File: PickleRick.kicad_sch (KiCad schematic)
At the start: 56 parts, among them J1 RBUS, J12 Conn_01x03_Male, J2 Conn_01x02_Male, J3 292227-7, J4 Micro_SD_Card_Det, Q1 PMV20ENR, U1 ESP32-S3, U2 DPS310, Y1 40MHz±10ppm

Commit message: all components basically routed and fitted onto pickle v2
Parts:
- R34, R35: footprint (none) -> Resistor_SMD:R_0402_1005Metric
- U2: footprint XDCR_DPS310 -> iclr:XDCR_DPS310
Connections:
- net BARO_CS: now also U1.19 (GPIO14/ADC2_CH3); no longer U1.12 (GPIO7/ADC1_CH6)
- net HSPI_MISO: now also U1.39 (GPIO34); no longer U1.40 (GPIO35)
- net HSPI_MOSI: now also U1.38 (GPIO33); no longer U1.39 (GPIO34)
- net HSPI_SCLK: now also U1.40 (GPIO35); no longer U1.38 (GPIO33)
- net IMU1_CS: now also U1.17 (GPIO12/ADC2_CH1); no longer U1.11 (GPIO6/ADC1_CH5)
- net IMU2_CS: now also U1.16 (GPIO11/ADC2_CH0); no longer U1.10 (GPIO5/ADC1_CH4)
- net LORA_CS: now also U1.15 (GPIO10/ADC1_CH9); no longer U1.13 (GPIO8/ADC1_CH7)
- net LORA_INT: now also U1.10 (GPIO5/ADC1_CH4); no longer U1.15 (GPIO10/ADC1_CH9)
- net MAG_CS: now also U1.18 (GPIO13/ADC2_CH2); no longer U1.9 (GPIO4/ADC1_CH3)
- net SD1_CS: now also U1.9 (GPIO4/ADC1_CH3); no longer U1.19 (GPIO14/ADC2_CH3)
- net SD1_DET: now also U1.11 (GPIO6/ADC1_CH5); no longer U1.18 (GPIO13/ADC2_CH2)
- net SD2_CS: now also U1.13 (GPIO8/ADC1_CH7); no longer U1.17 (GPIO12/ADC2_CH1)
- net SD2_DET: now also U1.12 (GPIO7/ADC1_CH6); no longer U1.16 (GPIO11/ADC2_CH0)
- net VSPI_MISO: now also J3.6, U1.43 (GPIO38); no longer J3.3, U1.41 (GPIO36)
- net VSPI_MOSI: now also J3.3, U1.41 (GPIO36); no longer J3.6, U1.43 (GPIO38)
- net power/RBUS_3.3_IN renamed power/RBUS_3.3V_IN
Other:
- sheet power ports: added RBUS_3.3V_IN; removed RBUS_3.3_IN
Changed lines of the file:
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@@
     (effects (font (size 1.27 1.27)) (justify left bottom))
   )
-  (label "IMU1_CS" (at 60.96 85.09 180)
+  (label "SD1_DET" (at 60.96 85.09 180)
     (effects (font (size 1.27 1.27)) (justify right bottom))
   )
@@
     (effects (font (size 1.27 1.27)) (justify left bottom))
   )
-  (label "VSPI_MISO" (at 243.84 30.48 0)
-    (effects (font (size 1.27 1.27)) (justify left bottom))
-  )
-  (label "SD2_CS" (at 60.96 100.33 180)
-    (effects (font (size 1.27 1.27)) (justify right bottom))
-  )
-  (label "LORA_INT" (at 60.96 95.25 180)
+  (label "VSPI_MOSI" (at 243.84 30.48 0)
+    (effects (font (size 1.27 1.27)) (justify left bottom))
+  )
+  (label "IMU1_CS" (at 60.96 100.33 180)
+    (effects (font (size 1.27 1.27)) (justify right bottom))
+  )
+  (label "LORA_CS" (at 60.96 95.25 180)
     (effects (font (size 1.27 1.27)) (justify right bottom))
   )
@@
     (effects (font (size 1.27 1.27)) (justify left bottom))
   )
-  (label "VSPI_MISO" (at 143.51 102.87 0)
+  (label "VSPI_MOSI" (at 143.51 102.87 0)
     (effects (font (size 1.27 1.27)) (justify left bottom))
   )
@@
     (effects (font (size 1.27 1.27)) (justify left bottom))
   )
-  (label "MAG_CS" (at 60.96 80.01 180)
+  (label "SD1_CS" (at 60.96 80.01 180)
     (effects (font (size 1.27 1.27)) (justify right bottom))
   )
@@
     (effects (font (size 1.27 1.27)) (justify left bottom))
   )
-  (label "VSPI_MOSI" (at 143.51 107.95 0)
+  (label "VSPI_MISO" (at 143.51 107.95 0)
     (effects (font (size 1.27 1.27)) (justify left bottom))
   )
@@
     (effects (font (size 1.27 1.27)) (justify left bottom))
   )
-  (label "HSPI_SCLK" (at 143.51 95.25 0)
-    (effects (font (size 1.27 1.27)) (justify left bottom))
-  )
-  (label "LORA_CS" (at 60.96 90.17 180)
+  (label "HSPI_MOSI" (at 143.51 95.25 0)
+    (effects (font (size 1.27 1.27)) (justify left bottom))
+  )
+  (label "SD2_CS" (at 60.96 90.17 180)
     (effects (font (size 1.27 1.27)) (justify right bottom))
   )
@@
     (effects (font (size 1.27 1.27)) (justify left bottom))
   )
-  (label "HSPI_MISO" (at 143.51 100.33 0)
+  (label "HSPI_SCLK" (at 143.51 100.33 0)
     (effects (font (size 1.27 1.27)) (justify left bottom))
   )
@@
     (effects (font (size 1.27 1.27)) (justify left bottom))
   )
-  (label "IMU2_CS" (at 60.96 82.55 180)
-    (effects (font (size 1.27 1.27)) (justify right bottom))
-  )
-  (label "HSPI_MOSI" (at 143.51 97.79 0)
-    (effects (font (size 1.27 1.27)) (justify left bottom))
-  )
-  (label "BARO_CS" (at 60.96 87.63 180)
+  (label "LORA_INT" (at 60.96 82.55 180)
+    (effects (font (size 1.27 1.27)) (justify right bottom))
+  )
+  (label "HSPI_MISO" (at 143.51 97.79 0)
+    (effects (font (size 1.27 1.27)) (justify left bottom))
+  )
+  (label "SD2_DET" (at 60.96 87.63 180)
     (effects (font (size 1.27 1.27)) (justify right bottom))
   )
@@
     (effects (font (size 1.27 1.27)) (justify right bottom))
   )
-  (label "SD1_CS" (at 60.96 105.41 180)
-    (effects (font (size 1.27 1.27)) (justify right bottom))
-  )
-  (label "VSPI_MOSI" (at 243.84 38.1 0)
+  (label "BARO_CS" (at 60.96 105.41 180)
+    (effects (font (size 1.27 1.27)) (justify right bottom))
+  )
+  (label "VSPI_MISO" (at 243.84 38.1 0)
     (effects (font (size 1.27 1.27)) (justify left bottom))
   )
@@
     (effects (font (size 1.27 1.27)) (justify left bottom))
   )
-  (label "SD2_DET" (at 60.96 97.79 180)
+  (label "IMU2_CS" (at 60.96 97.79 180)
     (effects (font (size 1.27 1.27)) (justify right bottom))
   )
@@
     (effects (font (size 1.27 1.27)) (justify left bottom))
   )
-  (label "SD1_DET" (at 60.96 102.87 180)
+  (label "MAG_CS" (at 60.96 102.87 180)
     (effects (font (size 1.27 1.27)) (justify right bottom))
   )
@@
       (effects (font (size 1.27 1.27)) (justify right))
     )
-    (property "Footprint" "" (id 2) (at 255.27 143.51 0)
+    (property "Footprint" "Resistor_SMD:R_0402_1005Metric" (id 2) (at 255.27 143.51 0)
       (effects (font (size 1.27 1.27)) hide)
     )
@@
       (effects (font (size 1.27 1.27)) (justify right))
     )
-    (property "Footprint" "" (id 2) (at 260.35 143.51 0)
+    (property "Footprint" "Resistor_SMD:R_0402_1005Metric" (id 2) (at 260.35 143.51 0)
       (effects (font (size 1.27 1.27)) hide)
     )
@@
     (property "Reference" "U2" (id 0) (at 250.19 102.87 0))
     (property "Value" "DPS310" (id 1) (at 250.19 105.41 0))
-    (property "Footprint" "XDCR_DPS310" (id 2) (at 250.19 120.65 0)
+    (property "Footprint" "iclr:XDCR_DPS310" (id 2) (at 250.19 120.65 0)
       (effects (font (size 1.27 1.27)) (justify bottom) hide)
     )
@@
       (effects (font (size 1.27 1.27)) (justify left))
     )
-    (pin "RBUS_3.3_IN" input (at 119.38 26.67 180)
+    (pin "RBUS_3.3V_IN" input (at 119.38 26.67 180)
       (effects (font (size 1.27 1.27)) (justify left))
     )
@@
     )
     (path "/ca0eab8e-e3fd-464d-bb03-d1603b8a651b/755f7a4b-a56d-4d46-9756-c8f6d0fad6ca"
-      (reference "R17") (unit 1) (value "500") (footprint "Resistor_SMD:R_0603_1608Metric")
+      (reference "R17") (unit 1) (value "500") (footprint "Resistor_SMD:R_0402_1005Metric")
     )
     (path "/ca0eab8e-e3fd-464d-bb03-d1603b8a651b/d2de353e-901e-432e-8627-a1b97e994765"
-      (reference "R18") (unit 1) (value "500") (footprint "Resistor_SMD:R_0603_1608Metric")
+      (reference "R18") (unit 1) (value "500") (footprint "Resistor_SMD:R_0402_1005Metric")
     )
     (path "/ca0eab8e-e3fd-464d-bb03-d1603b8a651b/09e6991d-9281-472b-b68c-4275861534b7"
@@
     )
     (path "/ca0eab8e-e3fd-464d-bb03-d1603b8a651b/c4d9bc73-27a3-45e8-9f5d-4537c1fd0ae5"
-      (reference "R21") (unit 1) (value "500") (footprint "Resistor_SMD:R_0603_1608Metric")
+      (reference "R21") (unit 1) (value "500") (footprint "Resistor_SMD:R_0402_1005Metric")
     )
     (path "/ca0eab8e-e3fd-464d-bb03-d1603b8a651b/24badbae-eef7-4d2c-a598-610e488ef81e"
-      (reference "R22") (unit 1) (value "500") (footprint "Resistor_SMD:R_0603_1608Metric")
+      (reference "R22") (unit 1) (value "500") (footprint "Resistor_SMD:R_0402_1005Metric")
     )
     (path "/ca0eab8e-e3fd-464d-bb03-d1603b8a651b/e4ae5c4e-e3f6-4ed9-b103-ab6e6ce37889"
@@
     )
     (path "/177d953f-3629-4fb8-8514-a9b0a91946a8"
-      (reference "R34") (unit 1) (value "4.7k") (footprint "")
+      (reference "R34") (unit 1) (value "4.7k") (footprint "Resistor_SMD:R_0402_1005Metric")
     )
     (path "/81f99459-3715-4203-a020-d8351a4eee55"
-      (reference "R35") (unit 1) (value "4.7k") (footprint "")
+      (reference "R35") (unit 1) (value "4.7k") (footprint "Resistor_SMD:R_0402_1005Metric")
     )
     (path "/c2e1c0d9-d402-4bd4-a6a0-62ddeebb3565"
@@
     )
     (path "/150d7a0e-7d8c-4788-bc30-4a3682bf4d09/268b5def-07ff-4842-bca3-d3886d833ee9"
-      (reference "TP10") (unit 1) (value "TestPoint") (footprint "TestPoint:TestPoint_Pad_D1.5mm")
+      (reference "TP10") (unit 1) (value "TestPoint") (footprint "TestPoint:TestPoint_Pad_D1.0mm")
     )
     (path "/150d7a0e-7d8c-4788-bc30-4a3682bf4d09/191a622e-bbb5-4124-b7c1-abd7ab78da85"
-      (reference "TP11") (unit 1) (value "TestPoint") (footprint "TestPoint:TestPoint_Pad_D1.5mm")
+      (reference "TP11") (unit 1) (value "TestPoint") (footprint "TestPoint:TestPoint_Pad_D1.0mm")
     )
     (path "/150d7a0e-7d8c-4788-bc30-4a3682bf4d09/6b63f8e0-062c-443a-b458-4bc92c46512c"
-      (reference "TP12") (unit 1) (value "TestPoint") (footprint "TestPoint:TestPoint_Pad_D1.5mm")
+      (reference "TP12") (unit 1) (value "TestPoint") (footprint "TestPoint:TestPoint_Pad_D1.0mm")
     )
     (path "/150d7a0e-7d8c-4788-bc30-4a3682bf4d09/0870865b-0b96-41ff-bd58-be45e025f47e"
-      (reference "TP13") (unit 1) (value "TestPoint") (footprint "TestPoint:TestPoint_Pad_D1.5mm")
+      (reference "TP13") (unit 1) (value "TestPoint") (footprint "TestPoint:TestPoint_Pad_D1.0mm")
     )
     (path "/150d7a0e-7d8c-4788-bc30-4a3682bf4d09/7ed4ea5d-2ecf-42be-88a1-8b4cc9b70ab6"
-      (reference "TP14") (unit 1) (value "TestPoint") (footprint "TestPoint:TestPoint_Pad_D1.5mm")
+      (reference "TP14") (unit 1) (value "TestPoint") (footprint "TestPoint:TestPoint_Pad_D1.0mm")
     )
     (path "/53a382a5-9123-45f3-a2e9-3b2de6ca541d/765637ac-b392-4de9-bfe2-ec35604f0b7c"
@@
     )
     (path "/a53547c8-4347-46fd-a668-dd224bf6ff89"
-      (reference "U2") (unit 1) (value "DPS310") (footprint "XDCR_DPS310")
+      (reference "U2") (unit 1) (value "DPS310") (footprint "iclr:XDCR_DPS310")
     )
     (path "/ca0eab8e-e3fd-464d-bb03-d1603b8a651b/c54e645d-6515-448d-a61f-0a3d4effdf3a"

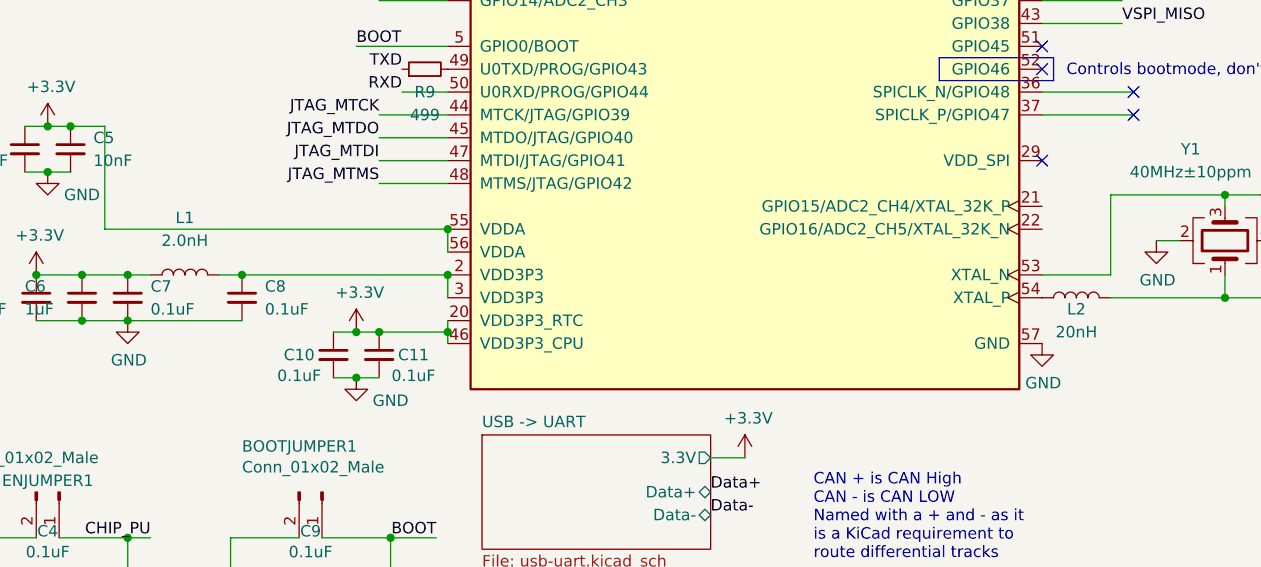
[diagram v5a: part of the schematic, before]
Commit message: changed bb and power side
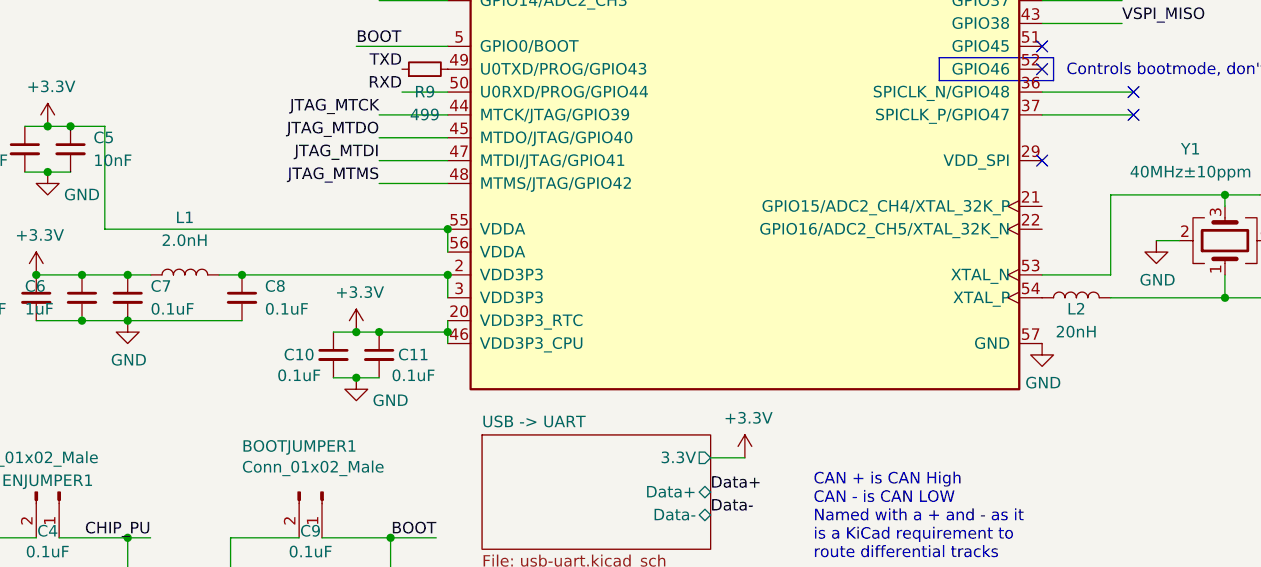
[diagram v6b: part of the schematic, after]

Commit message: layout almost complete
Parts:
- added TP12, TP14, TP18, TP19, TP20, TP21, TP22, TP23, TP25, TP26, TP27, TP28: TestPoint, TestPoint:TestPoint_Pad_D1.0mm, symbol Connector:TestPoint
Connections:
- net BARO_CS: now also TP28.1
- net HSPI_MISO: now also TP14.1
- net HSPI_MOSI: now also TP12.1
- net HSPI_SCLK: now also TP18.1
- net IMU1_CS: now also TP26.1
- net IMU2_CS: now also TP25.1
- net MAG_CS: now also TP27.1
- net RXD: now also TP22.1
- net TXD: now also TP23.1
- net VSPI_MISO: now also TP21.1
- net VSPI_MOSI: now also TP19.1
- net VSPI_SCLK: now also TP20.1

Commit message: imagine fixing your DRC errors
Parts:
- C12: value 4.2pF -> DNP
- C13, C14: value C -> 11pF
- R8: value 47.5 -> DNP
- Y1: value 40MHz±10ppm -> R940000171
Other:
- note removed: "TBD C and R value to get a total series impedance of 50 ohms at 2.4GHz"
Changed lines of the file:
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@@
     (stroke (width 0) (type default))
   )
+  (text_box "Crystal must be 40 MHz and at least ±10ppm"
+    (at 142.24 139.7 0) (size 19.05 11.43)
+    (stroke (width -0.0001) (type default))
+    (fill (type none))
+    (effects (font (size 1.27 1.27)) (justify left top))
+  )
   (text "Controls JTAG source, don't use\n" (at 65.8157 78.0878 0)
     (effects (font (size 1.27 1.27)) (justify right bottom))
-  )
-  (text "TBD C and R value to get\na total series impedance\nof 50 ohms at 2.4GHz\n"
-    (at 43.18 55.88 0)
-    (effects (font (size 1.27 1.27)) (justify left bottom))
   )
   (text "CAN + is CAN High\nCAN - is CAN LOW\nNamed with a + and - as it\nis a KiCad requirement to\nroute differential tracks\n"
@@
       (effects (font (size 1.27 1.27)))
     )
-    (property "Value" "47.5" (at 55.88 59.69 90)
+    (property "Value" "DNP" (at 55.88 59.69 90)
       (effects (font (size 1.27 1.27)))
     )
@@
       (effects (font (size 1.27 1.27)) (justify left))
     )
-    (property "Value" "4.2pF" (at 67.31 59.69 90)
+    (property "Value" "DNP" (at 67.31 59.69 90)
       (effects (font (size 1.27 1.27)) (justify left))
     )
@@
       (effects (font (size 1.27 1.27)) (justify left))
     )
-    (property "Value" "C" (at 163.83 144.5514 90)
+    (property "Value" "11pF" (at 163.83 144.5514 90)
       (effects (font (size 1.27 1.27)) (justify left))
     )
@@
       (effects (font (size 1.27 1.27)) (justify left))
     )
-    (property "Value" "C" (at 162.56 124.2314 90)
+    (property "Value" "11pF" (at 162.56 124.2314 90)
       (effects (font (size 1.27 1.27)) (justify left))
     )
@@
   (symbol (lib_id "Device:Crystal_GND24") (at 154.94 132.08 90) (unit 1)
     (in_bom yes) (on_board yes) (dnp no)
-    (property "Reference" "Y1" (at 151.13 121.92 90)
-      (effects (font (size 1.27 1.27)))
-    )
-    (property "Value" "40MHz±10ppm" (at 151.13 124.46 90)
-      (effects (font (size 1.27 1.27)))
-    )
+    (property "Reference" "Y1" (at 148.59 121.92 90)
+      (effects (font (size 1.27 1.27)))
+    )
+    (property "Value" "R940000171" (at 148.59 124.46 90)
+      (effects (font (size 1.27 1.27)))
+    )
